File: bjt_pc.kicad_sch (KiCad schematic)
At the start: 67 parts, among them J1 Conn_02x10_Odd_Even

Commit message: Finalized compressed 1.0
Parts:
- Qand11, Qand12, Qand13, Qand21, Qand22, Qand23, Qbuf1, Qbuf2, Qmux1, Qmux2, Qmux3, Qmux4, Qmux5, Qmux6, Qsrl1, Qsrl2, Qsrl3, Qtsb2, Qtsb3, Qtsb4, Qtsb5, Qtsb6: footprint Custom_Footprints:TO-92_Inline_disp -> Package_TO_SOT_THT:TO-92_Inline_Wide
- Qtsb1: footprint Custom_Footprints:TO-92_Inline_PNP_disp -> Package_TO_SOT_THT:TO-92_Inline_Wide
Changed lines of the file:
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@@
 			)
 		)
-		(property "Footprint" "Custom_Footprints:TO-92_Inline_disp"
+		(property "Footprint" "Package_TO_SOT_THT:TO-92_Inline_Wide"
 			(at 533.4 130.81 0)
 			(effects
@@
 			)
 		)
-		(property "Footprint" "Custom_Footprints:TO-92_Inline_disp"
+		(property "Footprint" "Package_TO_SOT_THT:TO-92_Inline_Wide"
 			(at 278.13 125.73 0)
 			(effects
@@
 			)
 		)
-		(property "Footprint" "Custom_Footprints:TO-92_Inline_disp"
+		(property "Footprint" "Package_TO_SOT_THT:TO-92_Inline_Wide"
 			(at 632.46 128.27 0)
 			(effects
@@
 			)
 		)
-		(property "Footprint" "Custom_Footprints:TO-92_Inline_disp"
+		(property "Footprint" "Package_TO_SOT_THT:TO-92_Inline_Wide"
 			(at 382.27 125.73 0)
 			(effects
@@
 			)
 		)
-		(property "Footprint" "Custom_Footprints:TO-92_Inline_disp"
+		(property "Footprint" "Package_TO_SOT_THT:TO-92_Inline_Wide"
 			(at 172.72 147.32 0)
 			(effects
@@
 			)
 		)
-		(property "Footprint" "Custom_Footprints:TO-92_Inline_disp"
+		(property "Footprint" "Package_TO_SOT_THT:TO-92_Inline_Wide"
 			(at 353.06 115.57 0)
 			(effects
@@
 			)
 		)
-		(property "Footprint" "Custom_Footprints:TO-92_Inline_disp"
+		(property "Footprint" "Package_TO_SOT_THT:TO-92_Inline_Wide"
 			(at 353.06 133.35 0)
 			(effects
@@
 			)
 		)
-		(property "Footprint" "Custom_Footprints:TO-92_Inline_disp"
+		(property "Footprint" "Package_TO_SOT_THT:TO-92_Inline_Wide"
 			(at 457.2 125.73 0)
 			(effects
@@
 			)
 		)
-		(property "Footprint" "Custom_Footprints:TO-92_Inline_disp"
+		(property "Footprint" "Package_TO_SOT_THT:TO-92_Inline_Wide"
 			(at 566.42 125.73 0)
 			(effects
@@
 			)
 		)
-		(property "Footprint" "Custom_Footprints:TO-92_Inline_disp"
+		(property "Footprint" "Package_TO_SOT_THT:TO-92_Inline_Wide"
 			(at 751.84 118.11 0)
 			(effects
@@
 			)
 		)
-		(property "Footprint" "Custom_Footprints:TO-92_Inline_disp"
+		(property "Footprint" "Package_TO_SOT_THT:TO-92_Inline_Wide"
 			(at 309.88 125.73 0)
 			(effects
@@
 			)
 		)
-		(property "Footprint" "Custom_Footprints:TO-92_Inline_disp"
+		(property "Footprint" "Package_TO_SOT_THT:TO-92_Inline_Wide"
 			(at 427.99 115.57 0)
 			(effects
@@
 			)
 		)
-		(property "Footprint" "Custom_Footprints:TO-92_Inline_disp"
+		(property "Footprint" "Package_TO_SOT_THT:TO-92_Inline_Wide"
 			(at 427.99 133.35 0)
 			(effects
@@
 			)
 		)
-		(property "Footprint" "Custom_Footprints:TO-92_Inline_disp"
+		(property "Footprint" "Package_TO_SOT_THT:TO-92_Inline_Wide"
 			(at 193.04 128.27 0)
 			(effects
@@
 			)
 		)
-		(property "Footprint" "Custom_Footprints:TO-92_Inline_disp"
+		(property "Footprint" "Package_TO_SOT_THT:TO-92_Inline_Wide"
 			(at 508 130.81 0)
 			(effects
@@
 			)
 		)
-		(property "Footprint" "Custom_Footprints:TO-92_Inline_disp"
+		(property "Footprint" "Package_TO_SOT_THT:TO-92_Inline_Wide"
 			(at 688.34 120.65 0)
 			(effects
@@
 			)
 		)
-		(property "Footprint" "Custom_Footprints:TO-92_Inline_disp"
+		(property "Footprint" "Package_TO_SOT_THT:TO-92_Inline_Wide"
 			(at 731.52 128.27 0)
 			(effects
@@
 			)
 		)
-		(property "Footprint" "Custom_Footprints:TO-92_Inline_disp"
+		(property "Footprint" "Package_TO_SOT_THT:TO-92_Inline_Wide"
 			(at 605.79 128.27 0)
 			(effects
@@
 			)
 		)
-		(property "Footprint" "Custom_Footprints:TO-92_Inline_disp"
+		(property "Footprint" "Package_TO_SOT_THT:TO-92_Inline_Wide"
 			(at 688.34 107.95 0)
 			(effects
@@
 			)
 		)
-		(property "Footprint" "Custom_Footprints:TO-92_Inline_disp"
+		(property "Footprint" "Package_TO_SOT_THT:TO-92_Inline_Wide"
 			(at 713.74 128.27 0)
 			(effects
@@
 			)
 		)
-		(property "Footprint" "Custom_Footprints:TO-92_Inline_PNP_disp"
+		(property "Footprint" "Package_TO_SOT_THT:TO-92_Inline_Wide"
 			(at 751.84 101.6 0)
 			(effects
@@
 			)
 		)
-		(property "Footprint" "Custom_Footprints:TO-92_Inline_disp"
+		(property "Footprint" "Package_TO_SOT_THT:TO-92_Inline_Wide"
 			(at 234.95 127 0)
 			(effects
@@
 			)
 		)
-		(property "Footprint" "Custom_Footprints:TO-92_Inline_disp"
+		(property "Footprint" "Package_TO_SOT_THT:TO-92_Inline_Wide"
 			(at 234.95 146.05 0)
 			(effects

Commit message: Added Test Points
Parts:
- added TP1, TP2, TP3, TP4, TP5: TestPoint, TestPoint:TestPoint_THTPad_D3.0mm_Drill1.5mm, symbol Connector:TestPoint
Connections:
- net DATA: now also TP4.1
- net R: now also TP3.1
- net S: now also TP2.1
- net at Qmux2.3 (C), R27.1, R30.1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: now also TP1.1
- net at Qsrl2.3 (C), R13.1, R14.2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: now also TP5.1

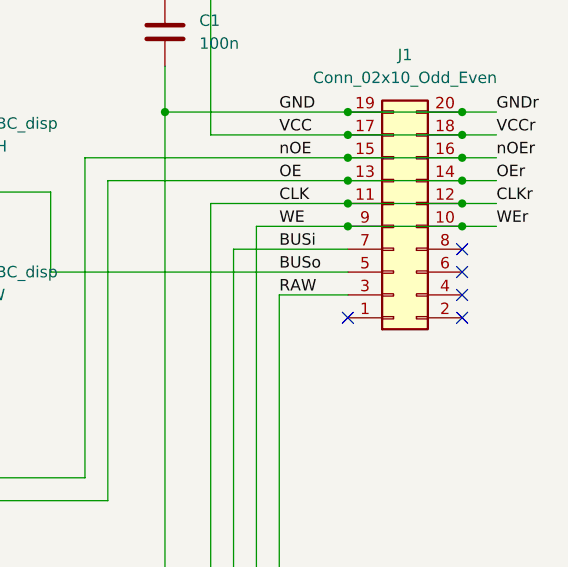
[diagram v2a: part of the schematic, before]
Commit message: Added back silkscreen stuff
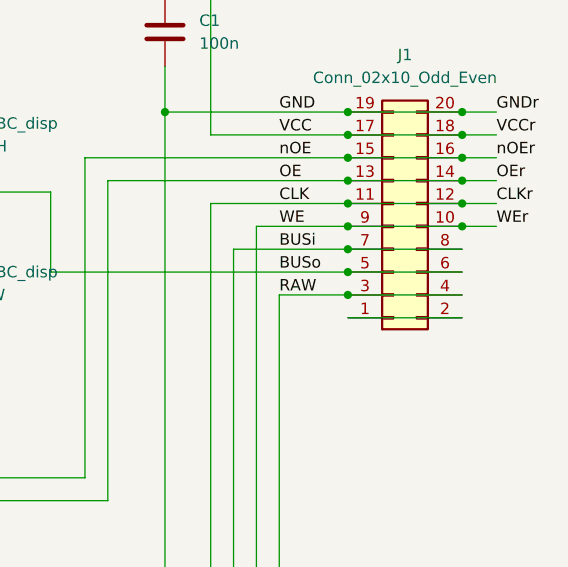
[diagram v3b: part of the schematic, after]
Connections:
- net BUSi: now also J1.8 (Pin_8)
- net BUSo: now also J1.6 (Pin_6)
- net RAW: now also J1.4 (Pin_4)
- net at J1.1 (Pin_1): now also J1.2 (Pin_2)
- no-connect marks 5 -> 0
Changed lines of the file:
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@@
+	)
+	(junction
+		(at 798.83 121.92)
+		(diameter 0)
+		(color 0 0 0 0)
 	)
 	(junction
@@
 	)
 	(junction
+		(at 798.83 124.46)
+		(diameter 0)
+		(color 0 0 0 0)
+	)
+	(junction
 		(at 811.53 111.76)
 		(diameter 0)
@@
 	)
 	(junction
+		(at 798.83 119.38)
+		(diameter 0)
+		(color 0 0 0 0)
+	)
+	(junction
 		(at 811.53 116.84)
 		(diameter 0)
@@
 		(color 0 0 0 0)
 	)
-	(no_connect
-		(at 811.53 127)
-	)
-	(no_connect
-		(at 811.53 121.92)
-	)
-	(no_connect
-		(at 811.53 124.46)
-	)
-	(no_connect
-		(at 811.53 119.38)
-	)
-	(no_connect
-		(at 798.83 127)
-	)
 	(wire
 		(pts
@@
 	(wire
 		(pts
+			(xy 798.83 127) (xy 811.53 127)
+		)
+		(stroke
+			(width 0)
+			(type default)
+		)
+	)
+	(wire
+		(pts
 			(xy 232.41 153.67) (xy 232.41 185.42)
 		)
@@
 	(wire
 		(pts
+			(xy 798.83 121.92) (xy 811.53 121.92)
+		)
+		(stroke
+			(width 0)
+			(type default)
+		)
+	)
+	(wire
+		(pts
+			(xy 798.83 124.46) (xy 811.53 124.46)
+		)
+		(stroke
+			(width 0)
+			(type default)
+		)
+	)
+	(wire
+		(pts
 			(xy 765.81 113.03) (xy 765.81 121.92)
 		)
@@
 		)
 		(stroke
+			(width 0)
+			(type default)
+		)
+	)
+	(wire
+		(pts
+			(xy 798.83 119.38) (xy 811.53 119.38)
+		)
+		(stroke
